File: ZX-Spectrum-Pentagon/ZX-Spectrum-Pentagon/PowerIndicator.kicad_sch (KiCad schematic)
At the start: 14 parts

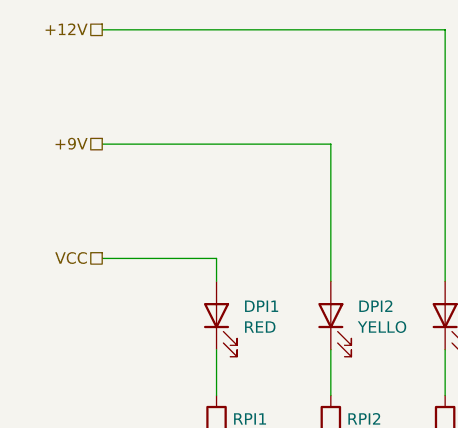
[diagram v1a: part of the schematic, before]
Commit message: FDControlers rename from VCC1 to VDD zx_custom_symbol add connector Conn_02x32_Odd_Even ZX-Spectrum-Pentagon rename from +9V to POWER ZX-Spectrum-Perefiral improve schematic
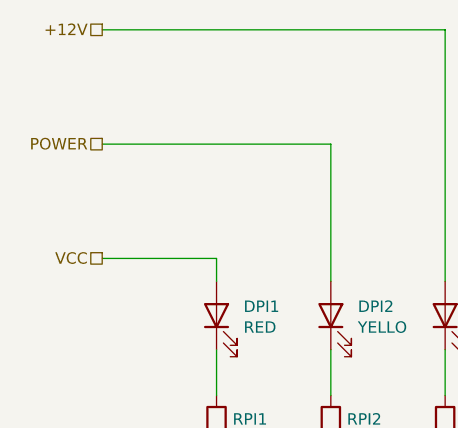
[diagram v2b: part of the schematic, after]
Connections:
- net +9V renamed POWER
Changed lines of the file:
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@@
 		)
 	)
-	(hierarchical_label "+9V"
+	(hierarchical_label "POWER"
 		(shape passive)
 		(at 25.4 38.1 180)
